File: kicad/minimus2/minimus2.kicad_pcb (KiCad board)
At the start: 2 copper layers, 0 parts

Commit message: start adding parts to schematic
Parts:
- added C1: C_Small, Capacitor_SMD:C_0402_1005Metric, F.Cu at (90.0, 102.0)
- added C2: C_Polarized_0402, Capacitor_SMD:C_0402_1005Metric, F.Cu at (109.8, 116.6)
- added C3: C_Polarized_0805, Capacitor_SMD:C_0805_2012Metric, F.Cu at (109.8, 108.1)
- added C4: C_Polarized_0603, Capacitor_SMD:C_0603_1608Metric, F.Cu at (109.8, 112.6)
- added D1: LED_Small, LED_SMD:LED_0402_1005Metric, F.Cu at (110.7, 96.5)
- added J1: PROG_SER, Connector_JST:JST_SH_BM06B-SRSS-TB_1x06-1MP_P1.00mm_Vertical, F.Cu at (97.7, 81.2)
- added LS1: SMT-0440-S-R, minimus:SMT-0440-S-R, F.Cu at (103.0, 94.0)
- added Q1: DMN3051L, Package_TO_SOT_SMD:SOT-23, F.Cu at (97.3, 98.6)
- added Q2: AO3401A, Package_TO_SOT_SMD:SOT-23, F.Cu at (102.9, 105.5)
- added R1: R_Small, Resistor_SMD:R_0402_1005Metric, F.Cu at (108.8, 96.6)
- added R2: 10k, Resistor_SMD:R_0402_1005Metric, F.Cu at (109.5, 85.0)
- added SW1: SW_Push, minimus:EVPBB, F.Cu at (84.6, 114.6)
- added U1: DRV8835, Package_SON:WSON-12-1EP_3x2mm_P0.5mm_EP1x2.65_ThermalVias, F.Cu at (90.2, 91.8)
- added U2: LSM6DS3, Package_LGA:LGA-14_3x2.5mm_P0.5mm_LayoutBorder3x4y, F.Cu at (89.7, 84.8)
- added U4: AS5047D, Package_SO:TSSOP-14_4.4x5mm_P0.65mm, F.Cu at (121.1, 95.8)
- added U5: AS5047D, Package_SO:TSSOP-14_4.4x5mm_P0.65mm, F.Cu at (71.7, 95.1)
- added U6: STM32U575CITx, Package_QFP:LQFP-48_7x7mm_P0.5mm, F.Cu at (93.8, 112.5)
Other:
- board outline added: 38 x 50 mm

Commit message: update kiad files
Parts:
- added D2: LED_Small, LED_THT:LED_D3.0mm_Horizontal_O1.27mm_Z2.0mm_IRBlack, F.Cu at (86.7, 86.6)
- added D3: LED_Small, LED_THT:LED_D3.0mm_Horizontal_O1.27mm_Z2.0mm_IRBlack, F.Cu at (116.5, 88.0)
- added D4: LED_Small, LED_THT:LED_D3.0mm_Horizontal_O1.27mm_Z2.0mm_IRBlack, F.Cu at (91.8, 78.7)
- added D5: LED_Small, LED_THT:LED_D3.0mm_Horizontal_O1.27mm_Z2.0mm_IRBlack, F.Cu at (109.6, 76.8)
- added J4: Conn_01x01, minimus:Motor Red, F.Cu at (88.0, 106.5)
- added J5: Conn_01x01, minimus:Motor Blk, F.Cu at (89.5, 106.5)
- added J6: Conn_01x01, minimus:Motor Red, F.Cu at (111.0, 106.5)
- added J7: Conn_01x01, minimus:Motor Blk, F.Cu at (112.5, 106.5)
- added L1: 47uH, minimus:IFSC-1515AH-01, F.Cu at (84.5, 107.5)
- added L2: 47uH, minimus:IFSC-1515AH-01, F.Cu at (116.0, 107.5)
- added Q3: SFH309, LED_THT:LED_D3.0mm_Horizontal_O1.27mm_Z2.0mm_Clear, F.Cu at (86.5, 83.5)
- added Q4: SFH309, LED_THT:LED_D3.0mm_Horizontal_O1.27mm_Z2.0mm_Clear, F.Cu at (116.9, 85.5)
- added Q5: SFH309, LED_THT:LED_D3.0mm_Horizontal_O1.27mm_Z2.0mm_Clear, F.Cu at (89.3, 80.2)
- added Q6: SFH309, LED_THT:LED_D3.0mm_Horizontal_O1.27mm_Z2.0mm_Clear, F.Cu at (111.8, 77.8)
- added Q7: DMN3051L, Package_TO_SOT_SMD:SOT-23, F.Cu at (83.5, 92.0)
- added Q8: DMN3051L, Package_TO_SOT_SMD:SOT-23, F.Cu at (87.0, 92.0)
- added Q9: DMN3051L, Package_TO_SOT_SMD:SOT-23, F.Cu at (115.7, 79.1)
- added SW2: RESET, Button_Switch_SMD:SW_Push_1P1T_NO_CK_KMR2, F.Cu at (115.0, 115.0)
- LS1: value SMT-0440-S-R -> SMT-0340-T-R; footprint minimus:SMT-0440-S-R -> minimus:SMT-0340-T-R
- SW1: value SW_Push -> USER_A; footprint minimus:EVPBB -> Button_Switch_SMD:SW_Push_1P1T_NO_CK_KMR2
- U1: footprint Package_SON:WSON-12-1EP_3x2mm_P0.5mm_EP1x2.65_ThermalVias -> minimus:DRV8835
- U2: value LSM6DS3 -> LSM6DSRTR
- moved J1 35.6 mm to (104.5, 116.2)
- moved D1 26.8 mm to (100.0, 72.0)
- moved R2 23.4 mm to (103.0, 107.5)
- moved LS1 19.2 mm to (100.0, 75.0)
- moved Q2 19.1 mm to (116.5, 92.0), turned to 90 degrees
- moved U2 18.5 mm to (100.0, 100.1)
- moved Q1 17.0 mm to (113.0, 92.1), turned to 90 degrees
- moved R1 15.0 mm to (103.0, 110.5)
- moved U5 15.0 mm to (63.0, 107.4)
- moved U4 12.4 mm to (130.0, 104.5)
- moved C1 11.8 mm to (100.5, 107.5)
- moved U1 11.5 mm to (95.0, 102.2)
- moved C2 11.1 mm to (100.5, 110.5)
- moved C4 9.25 mm to (101.3, 109.0)
- moved C3 2.52 mm to (107.5, 109.0)
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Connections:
- U1 pad 1: unconnected-(U1-VM-Pad1) -> +BATT
- U1 pad 10: unconnected-(U1-AIN1-Pad10) -> L_MOT1
- U1 pad 12: unconnected-(U1-VCC-Pad12) -> +3.3V
- U1 pad 13: unconnected-(U1-GNDP-Pad13) -> GND
- U1 pad 2: unconnected-(U1-AOUT1-Pad2) -> Net-(U1-AOUT1)
- U1 pad 3: unconnected-(U1-AOUT2-Pad3) -> Net-(J5-Pin_1)
- U1 pad 4: unconnected-(U1-BOUT1-Pad4) -> Net-(U1-BOUT1)
- U1 pad 5: unconnected-(U1-BOUT2-Pad5) -> Net-(J7-Pin_1)
- U1 pad 6: unconnected-(U1-GND-Pad6) -> GND
- U1 pad 7: unconnected-(U1-BIN2-Pad7) -> R_MOT2
- U1 pad 8: unconnected-(U1-BIN1-Pad8) -> R_MOT1
- U1 pad 9: unconnected-(U1-AIN2-Pad9) -> L_MOT2
- U2 pad 6: Net-(U2-GND-Pad6) -> GND
- U2 pad 7: Net-(U2-GND-Pad6) -> GND
- U4 pad 13: unconnected-(U4-GND-Pad13) -> GND
- U5 pad 13: unconnected-(U5-GND-Pad13) -> GND
- U6 pad 23: Net-(U6-VSS-Pad23) -> GND
- U6 pad 35: Net-(U6-VSS-Pad23) -> GND
- U6 pad 47: Net-(U6-VSS-Pad23) -> GND
- U6 pad 8: unconnected-(U6-VSSA-Pad8) -> GND
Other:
- board size 38 x 50 mm -> 55.5 x 50 mm

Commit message: Rough place most parts
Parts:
- removed J4, J6: Conn_01x01, minimus:Motor Red
- removed J5, J7: Conn_01x01, minimus:Motor Blk
- removed the Q2 at (116.5, 92.0)
- removed Q6: SFH309, LED_THT:LED_D3.0mm_Horizontal_O1.27mm_Z2.0mm_Clear
- removed Q7, Q8, Q9: DMN3051L, Package_TO_SOT_SMD:SOT-23
- removed U6: STM32U575CITx, Package_QFP:LQFP-48_7x7mm_P0.5mm
- added C5: 100nF, Capacitor_SMD:C_0402_1005Metric, F.Cu at (97.0, 109.0)
- added C6: 100nF, Capacitor_SMD:C_0402_1005Metric, F.Cu at (94.5, 118.5)
- added C7: 4.7uF, Capacitor_SMD:C_0805_2012Metric, F.Cu at (97.5, 118.0)
- added C8: 100nF, Capacitor_SMD:C_0402_1005Metric, F.Cu at (108.5, 103.5)
- added D5: LED, LED_SMD:LED_0402_1005Metric, F.Cu at (104.1, 112.0)
- added J2: LM, Connector_PinHeader_2.00mm:PinHeader_1x02_P2.00mm_Vertical, F.Cu at (89.0, 104.5)
- added J3: LM, Connector_PinHeader_2.00mm:PinHeader_1x02_P2.00mm_Vertical, F.Cu at (109.0, 106.0)
- added LFE1: SFH4050, LED_THT:LED_D3.0mm_Horizontal_O1.27mm_Z2.0mm_IRBlack, F.Cu at (85.5, 90.1)
- added LSE1: SFH4050, LED_THT:LED_D3.0mm_Horizontal_O1.27mm_Z2.0mm_IRBlack, F.Cu at (108.3, 76.3)
- added LSS1: SFH309, LED_THT:LED_D3.0mm_Horizontal_O1.27mm_Z2.0mm_Clear, F.Cu at (110.5, 77.5)
- added NT1: NetTie_2, NetTie:NetTie-2_SMD_Pad0.5mm, F.Cu at (109.5, 118.5)
- added Q1: RSE, Package_TO_SOT_SMD:SOT-23, F.Cu at (111.9, 74.0)
- added Q3: LFE, Package_TO_SOT_SMD:SOT-23, F.Cu at (87.9, 93.0)
- added R10: 1k0, Resistor_SMD:R_0402_1005Metric, F.Cu at (85.5, 77.5)
- added R11: 47k, Resistor_SMD:R_0402_1005Metric, F.Cu at (83.5, 94.0)
- added R12: 47k, Resistor_SMD:R_0402_1005Metric, F.Cu at (85.5, 75.5)
- added R13: 1k0, Resistor_SMD:R_0402_1005Metric, F.Cu at (88.0, 108.5)
- added R14: 10k, Resistor_SMD:R_0402_1005Metric, F.Cu at (105.6, 103.5)
- added R15: 47k, Resistor_SMD:R_0402_1005Metric, F.Cu at (101.0, 106.0)
- added R16: 47k, Resistor_SMD:R_0402_1005Metric, F.Cu at (101.0, 108.0)
- added R17: 1k0, Resistor_SMD:R_0402_1005Metric, F.Cu at (83.0, 82.5)
- added R18: 1k0, Resistor_SMD:R_0402_1005Metric, F.Cu at (88.0, 76.0)
- added R19: 1k0, Resistor_SMD:R_0402_1005Metric, F.Cu at (109.0, 73.5)
- added R20: 1k0, Resistor_SMD:R_0402_1005Metric, F.Cu at (111.5, 93.0)
- added R21: 1k0, Resistor_SMD:R_0402_1005Metric, F.Cu at (111.8, 111.3)
- added R22: 1k0, Resistor_SMD:R_0402_1005Metric, F.Cu at (101.0, 110.0)
- added R23: 1k0, Resistor_SMD:R_0402_1005Metric, F.Cu at (101.0, 112.0)
- added R24: 1k0, Resistor_SMD:R_0402_1005Metric, F.Cu at (101.0, 114.0)
- added R25: 1k0, Resistor_SMD:R_0402_1005Metric, F.Cu at (101.0, 116.0)
- added R26: 1k0, Resistor_SMD:R_0402_1005Metric, F.Cu at (111.8, 109.3)
- added R3: 1k0, Resistor_SMD:R_0402_1005Metric, F.Cu at (114.5, 76.5)
- added R4: 1k0, Resistor_SMD:R_0402_1005Metric, F.Cu at (112.5, 90.5)
- added R5: 47k, Resistor_SMD:R_0402_1005Metric, F.Cu at (116.0, 77.5)
- added R6: 47k, Resistor_SMD:R_0402_1005Metric, F.Cu at (118.0, 90.0)
- added R7: 33R, Resistor_SMD:R_0402_1005Metric, F.Cu at (88.0, 89.0)
- added R8: 33R, Resistor_SMD:R_0402_1005Metric, F.Cu at (93.5, 72.0)
- added R9: 1k0, Resistor_SMD:R_0402_1005Metric, F.Cu at (83.5, 92.5)
- added RFS1: SFH309, LED_THT:LED_D3.0mm_Horizontal_O1.27mm_Z2.0mm_Clear, F.Cu at (115.5, 88.0)
- added RSE1: SFH4050, LED_THT:LED_D3.0mm_Horizontal_O1.27mm_Z2.0mm_IRBlack, F.Cu at (92.7, 78.5)
- added RSS1: SFH309, LED_THT:LED_D3.0mm_Horizontal_O1.27mm_Z2.0mm_Clear, F.Cu at (90.3, 79.7)
- added SW1: RESET, Button_Switch_SMD:SW_Push_1P1T_NO_CK_KMR2, F.Cu at (107.5, 100.2)
- added TP1: BOOT_SEL, TestPoint:TestPoint_Pad_D1.0mm, F.Cu at (98.5, 115.0)
- added U2: STM32U575CITx, Package_QFP:LQFP-48_7x7mm_P0.5mm, F.Cu at (92.2, 112.8)
- C1: value C_Small -> 4.7uF; footprint Capacitor_SMD:C_0402_1005Metric -> Capacitor_SMD:C_0805_2012Metric
- C2: value C_Polarized_0402 -> 100nF
- C3: value C_Polarized_0805 -> 100nF; footprint Capacitor_SMD:C_0805_2012Metric -> Capacitor_SMD:C_0402_1005Metric
- C4: value C_Polarized_0603 -> 100nF; footprint Capacitor_SMD:C_0603_1608Metric -> Capacitor_SMD:C_0402_1005Metric
- D1: value LED_Small -> LED
- D2, D3, D4: value LED_Small -> LED; footprint LED_THT:LED_D3.0mm_Horizontal_O1.27mm_Z2.0mm_IRBlack -> LED_SMD:LED_0402_1005Metric
- J1: footprint Connector_JST:JST_SH_BM06B-SRSS-TB_1x06-1MP_P1.00mm_Vertical -> Connector_PinHeader_1.27mm:PinHeader_2x03_P1.27mm_Vertical
- Q2: renamed from Q1; value DMN3051L -> RFE
- Q4: value SFH309 -> LSE; footprint LED_THT:LED_D3.0mm_Horizontal_O1.27mm_Z2.0mm_Clear -> Package_TO_SOT_SMD:SOT-23
- Q5: value SFH309 -> DMN3051L; footprint LED_THT:LED_D3.0mm_Horizontal_O1.27mm_Z2.0mm_Clear -> Package_TO_SOT_SMD:SOT-23
- R1: value R_Small -> 33R
- R2: value 10k -> 33R
- RFE1: renamed from D5; value LED_Small -> SFH4050
- SW3: renamed from SW2; value RESET -> USER_B
- moved LS1 40.4 mm to (110.4, 114.0)
- moved R1 38.9 mm to (108.5, 72.0)
- moved D1 37.5 mm to (88.0, 107.5)
- moved Q5 35.6 mm to (107.9, 110.5), turned to 0 degrees
- moved D4 33.7 mm to (104.1, 110.0), turned to 0 degrees
- moved Q4 29.5 mm to (89.9, 73.5), turned to 0 degrees
- moved D2 26.1 mm to (104.1, 106.0), turned to 0 degrees
- moved R2 25.8 mm to (118.0, 86.5)
- moved D3 23.5 mm to (104.1, 108.0), turned to 0 degrees
- moved C2 18.1 mm to (84.0, 118.0)
- moved C1 17.1 mm to (87.0, 118.0)
- moved C4 15.3 mm to (86.0, 110.5)
- moved C3 13.6 mm to (94.0, 107.0)
- moved RFE1 10.8 mm to (116.0, 85.5), turned to 172 degrees
- moved Q2 3.04 mm to (116.0, 92.6)
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- renumbered Q3 to LFS1, SW1 to SW2, U2 to U1, U1 to U3
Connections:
- C1 pad 1: unconnected-(C1-Pad1) -> +3.3VA
- C1 pad 2: unconnected-(C1-Pad2) -> GNDA
- C2 pad 1: unconnected-(C2-Pad1) -> +3.3VA
- C2 pad 2: unconnected-(C2-Pad2) -> GNDA
- C3 pad 1: unconnected-(C3-Pad1) -> +3.3V
- C3 pad 2: unconnected-(C3-Pad2) -> GND
- C4 pad 1: unconnected-(C4-Pad1) -> +3.3V
- C4 pad 2: unconnected-(C4-Pad2) -> GND
- D1 pad 1: unconnected-(D1-K-Pad1) -> Net-(D1-K)
- D1 pad 2: unconnected-(D1-A-Pad2) -> Net-(D1-A)
- D2 pad 1: unconnected-(D2-K-Pad1) -> Net-(D2-K)
- D3 pad 1: unconnected-(D3-K-Pad1) -> Net-(D3-K)
- D4 pad 1: unconnected-(D4-K-Pad1) -> Net-(D4-K)
- LFS1 pad 1: unconnected-(Q3-C-Pad1) -> +3.3VA
- LFS1 pad 2: unconnected-(Q3-E-Pad2) -> LFS
- LS1 pad 1: unconnected-(LS1-Pad1) -> +3.3V
- LS1 pad 2: unconnected-(LS1-Pad2) -> Net-(Q5-D)
- Q2 pad 1: unconnected-(Q1-G-Pad1) -> Net-(Q2-G)
- Q2 pad 2: unconnected-(Q1-S-Pad2) -> GND
- Q2 pad 3: unconnected-(Q1-D-Pad3) -> Net-(Q2-D)
- Q4 pad 1: unconnected-(Q4-C-Pad1) -> Net-(Q4-G)
- Q4 pad 2: unconnected-(Q4-E-Pad2) -> GND
- Q5 pad 1: unconnected-(Q5-C-Pad1) -> Net-(Q5-G)
- Q5 pad 2: unconnected-(Q5-E-Pad2) -> GND
- R1 pad 1: unconnected-(R1-Pad1) -> +5V
- R1 pad 2: unconnected-(R1-Pad2) -> Net-(RSE1-A)
- R2 pad 1: unconnected-(R2-Pad1) -> +5V
- R2 pad 2: unconnected-(R2-Pad2) -> Net-(RFE1-A)
- RFE1 pad 1: unconnected-(D5-K-Pad1) -> Net-(Q2-D)
- RFE1 pad 2: unconnected-(D5-A-Pad2) -> Net-(RFE1-A)
- SW2 pad 1: unconnected-(SW1-Pad1) -> SW_A
- SW2 pad 2: unconnected-(SW1-Pad2) -> +3.3V
- SW3 pad 1: unconnected-(SW2-Pad1) -> +3.3V
- SW3 pad 2: GND -> SW_B

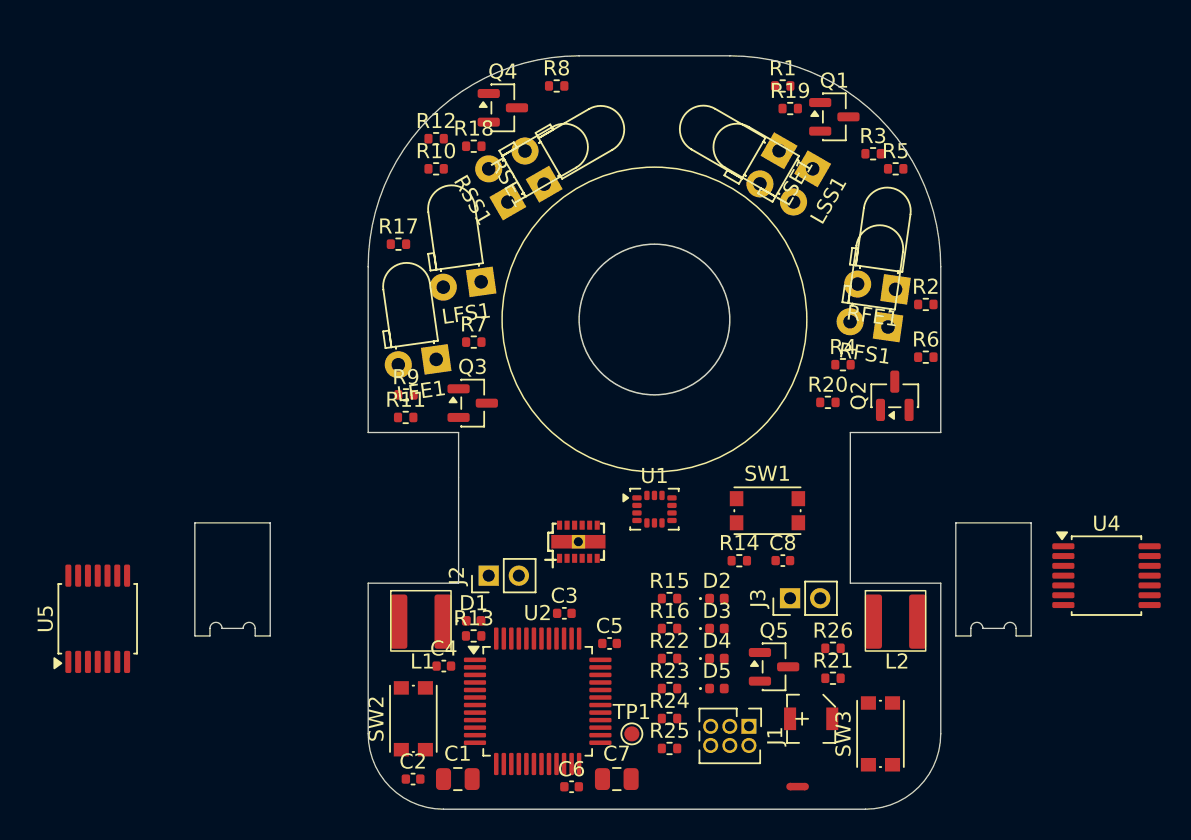
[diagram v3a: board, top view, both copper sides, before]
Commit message: add some parts libraries
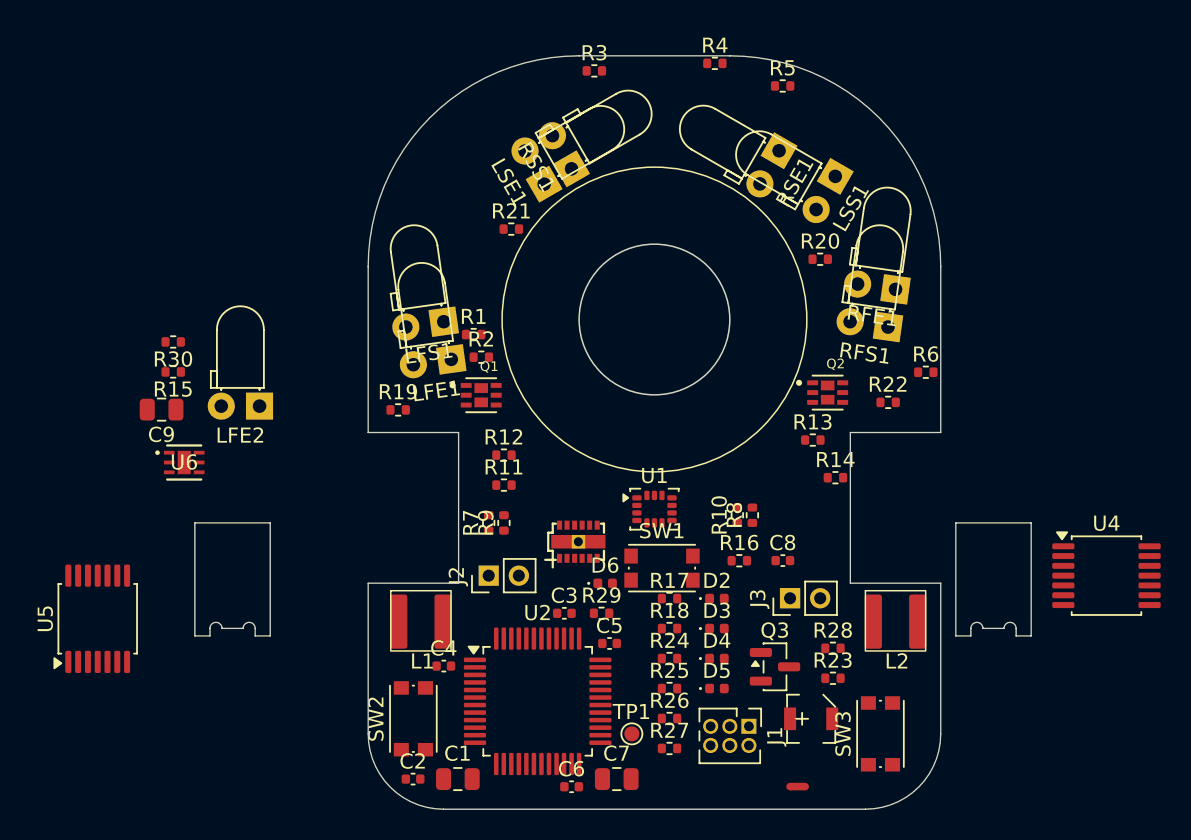
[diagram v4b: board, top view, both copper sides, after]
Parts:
- removed D1: LED, LED_SMD:LED_0402_1005Metric
- removed the Q3 at (87.9, 93.0)
- removed Q4: LSE, Package_TO_SOT_SMD:SOT-23
- removed the R5 at (116.0, 77.5)
- removed the R6 at (118.0, 90.0)
- added C9: 4.7uF, Capacitor_SMD:C_0805_2012Metric, F.Cu at (67.3, 93.5)
- added D6: LED, LED_SMD:LED_0402_1005Metric, F.Cu at (96.7, 105.0)
- added LFE2: SFH4050, LED_THT:LED_D3.0mm_Horizontal_O1.27mm_Z2.0mm_IRBlack, F.Cu at (73.8, 93.2)
- added R1: 33R, Resistor_SMD:R_0402_1005Metric, F.Cu at (88.0, 88.5)
- added R14: 47k, Resistor_SMD:R_0402_1005Metric, F.Cu at (112.0, 98.0)
- added R15: 5k6, Resistor_SMD:R_0402_1005Metric, F.Cu at (68.1, 91.0)
- added R2: 33R, Resistor_SMD:R_0402_1005Metric, F.Cu at (88.5, 90.0)
- added R29: 1k0, Resistor_SMD:R_0402_1005Metric, F.Cu at (96.5, 107.0)
- added R30: 5k6, Resistor_SMD:R_0402_1005Metric, F.Cu at (68.1, 89.0)
- added U6: BCR420UFD-7, BCR420UFD:U-DFN2020-6_2X2_DIO, F.Cu at (68.8, 97.0)
- Q1: value RSE -> SSM6N58NU_LF; footprint Package_TO_SOT_SMD:SOT-23 -> SSM6N58NU_LF:SON65P200X200X80-8N
- Q2: value RFE -> SSM6N58NU_LF; footprint Package_TO_SOT_SMD:SOT-23 -> SSM6N58NU_LF:SON65P200X200X80-8N
- R13: value 1k0 -> 47k
- R3, R4: value 1k0 -> 33R
- R7, R8: value 33R -> 1k0
- moved R8 31.3 mm to (106.5, 100.5), turned to 90 degrees
- moved R10 30.5 mm to (105.5, 100.5), turned to 90 degrees
- moved Q1 29.8 mm to (88.5, 92.5)
- moved R13 26.0 mm to (110.5, 95.5)
- moved R20 24.2 mm to (111.0, 83.5)
- moved R4 21.7 mm to (104.0, 70.5)
- moved R12 21.5 mm to (90.0, 96.5)
- moved R21 20.2 mm to (90.5, 81.5)
- moved R3 19.3 mm to (96.0, 71.0)
- moved R7 12.0 mm to (89.0, 101.0), turned to 90 degrees
- moved R19 11.0 mm to (83.0, 93.5)
- moved R9 10.7 mm to (90.0, 101.0), turned to 90 degrees
- moved SW1 7.97 mm to (100.5, 104.0)
- moved R11 7.92 mm to (90.0, 98.5)
- moved RSS1 4.77 mm to (94.5, 77.5)
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- renumbered RSE1 to LSE1, Q5 to Q3, R14 to R16, R15 to R17, R16 to R18, R17 to R19, R18 to R20, R19 to R21, R20 to R22, R21 to R23, R22 to R24, R23 to R25, R24 to R26, R25 to R27, R26 to R28, R1 to R5, R2 to R6, LSE1 to RSE1
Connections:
- net Net-(D1-A) renamed BOOT0
- D2 pad 2: unconnected-(D2-A-Pad2) -> LED1
- D3 pad 2: unconnected-(D3-A-Pad2) -> LED2
- D4 pad 2: unconnected-(D4-A-Pad2) -> LED3
- D5 pad 2: unconnected-(D5-A-Pad2) -> LED4
- LFE1 pad 2: Net-(LFE1-A) -> +5V
- LSE1 pad 1: Net-(Q1-D) -> Net-(LSE1-K)
- LSE1 pad 2: Net-(RSE1-A) -> +5V
- Q1 pad 1: Net-(Q1-G) -> GND
- Q1 pad 2: GND -> Net-(Q1-G1)
- Q1 pad 3: Net-(Q1-D) -> Net-(Q1-D2-Pad3)
- Q2 pad 1: Net-(Q2-G) -> Net-(Q2-S1)
- Q2 pad 3: Net-(Q2-D) -> Net-(Q2-D2-Pad3)
- R10 pad 2: Net-(Q4-G) -> GND
- R11 pad 1: Net-(Q3-G) (its old number) -> Net-(Q1-G2)
- R12 pad 1: Net-(Q4-G) -> Net-(Q1-G1)
- R13 pad 1: Net-(D1-K) -> Net-(Q2-S2)
- R3 pad 1: RSE -> Net-(LSE1-K)
- R3 pad 2: Net-(Q1-G) -> Net-(Q1-D1-Pad6)
- R4 pad 1: RFE -> Net-(RSE1-K)
- R4 pad 2: Net-(Q2-G) -> Net-(Q2-D2-Pad3)
- R5 pad 1: +5V -> Net-(LSE1-K)
- R5 pad 2: Net-(RSE1-A) -> Net-(Q2-D2-Pad3)
- R6 pad 1: +5V -> Net-(RFE1-K)
- R6 pad 2: Net-(RFE1-A) -> Net-(Q2-D1-Pad6)
- R7 pad 1: +5V -> RSE
- R7 pad 2: Net-(LFE1-A) -> Net-(Q1-G1)
- R8 pad 1: +5V -> RFE
- R8 pad 2: Net-(LSE1-A) -> GND
- R9 pad 2: Net-(Q3-G) (its old number) -> Net-(Q1-G2)
- RFE1 pad 1: Net-(Q2-D) -> Net-(RFE1-K)
- RFE1 pad 2: Net-(RFE1-A) -> +5V
- RSE1 pad 1: Net-(LSE1-K) -> Net-(RSE1-K)
- RSE1 pad 2: Net-(LSE1-A) -> +5V

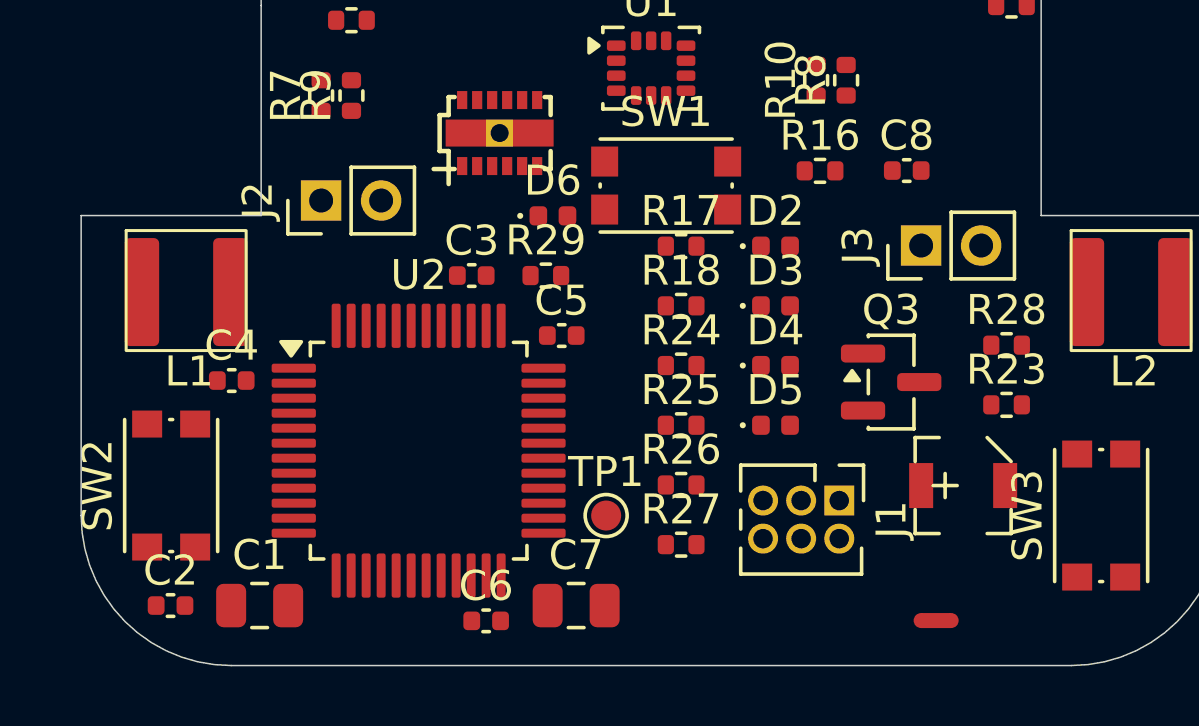
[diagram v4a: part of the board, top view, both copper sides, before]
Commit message: add 3D model for BCR420UFD
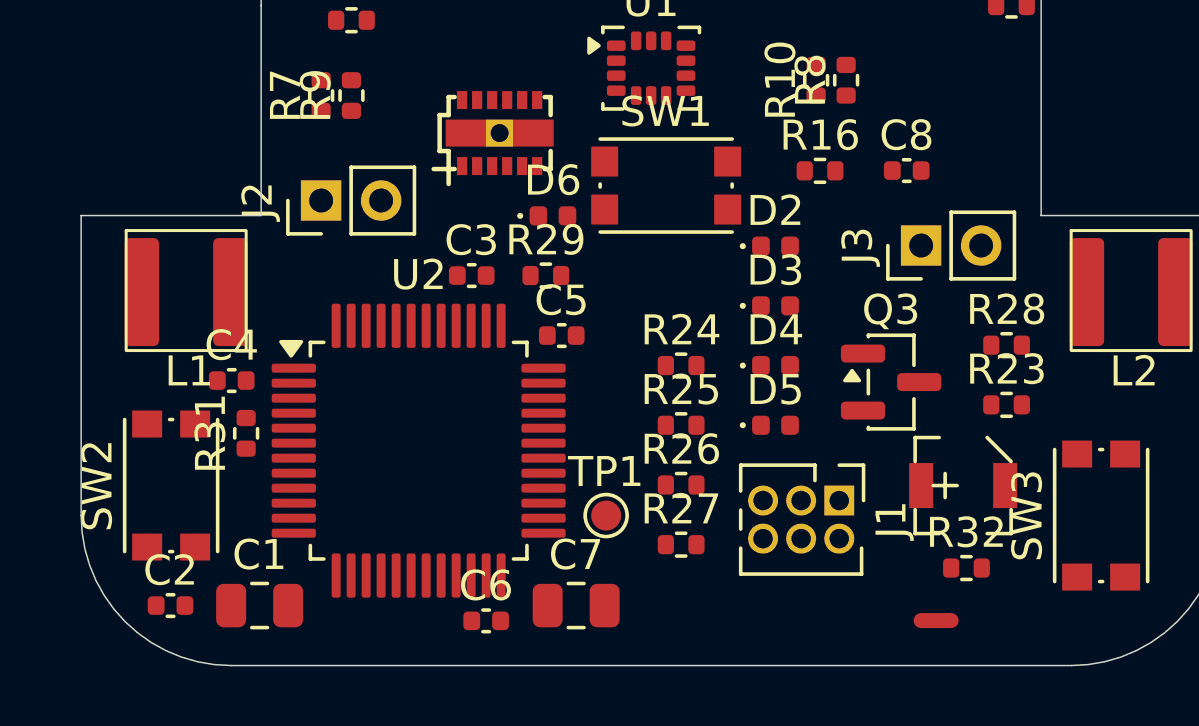
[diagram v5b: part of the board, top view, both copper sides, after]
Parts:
- removed R17, R18: 47k, Resistor_SMD:R_0402_1005Metric
- added R31: 47k, Resistor_SMD:R_0402_1005Metric, F.Cu at (86.5, 112.3)
- added R32: 47k, Resistor_SMD:R_0402_1005Metric, F.Cu at (110.5, 116.8)
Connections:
- SW2 pad 1: SW_A -> GND
- SW2 pad 2: +3.3V -> SW_A
- SW3 pad 1: +3.3V -> SW_B
- SW3 pad 2: SW_B -> GND
